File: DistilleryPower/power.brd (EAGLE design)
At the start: 50 x 86.9 mm, 31 parts, among them IC2 ACS758LCB-050B-PFF-T, J1 GREEN-2P-5.0, J2 GREEN-2P-5.0, Q1 BC807-16LT1SMD, T1 BT138-DSH, U1 STM32F042KXTX

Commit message: digital part schematics
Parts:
- added C10, C13: 10u/25, rcl:SMC_B
- added C11, C12: 20p, rcl:C0805
- added C14, C15, C18, C19, C6, C8: 0.1, rcl:C0805
- added C16, C17: (no value), rcl:C0805
- added C7: 100p, rcl:C0805
- added C9: 0.01/500, rcl:C1206
- added IC3: (no value), SparkFun:SOT223
- added IC4: ACS758LCB-050B-PFF-T, allegro:CB-PFF
- added J3, J4, J5: GREEN-2P-5.0, distillery:H2-5.0-10.5X8.0MM
- added R14: 220, rcl:R0805
- added R15: (no value), rcl:R0805
- added SV1: (no value), distillery:CON-LSTB_MA06-1
- added X1: IQD-FREQUENCY-PRODUCTS_CRYSTALS-NOGND-4-HSMX, distillery:IQD-FREQUENCY-PRODUCTS_HC49-4-HSMX
- C1: value 0.47/50 -> 0.1; device rcl:C/6032-28R -> rcl:C0805
- C2, C5: value (none) -> 0.1
- C3: value 0.01/500 -> 0.1; device rcl:C1206 -> rcl:C0805
- C4: value (none) -> 0.47/50; device rcl:C0805 -> rcl:C/6032-28R
- IC1: value (none) -> SN65HVD230/1; device SparkFun:SOT223 -> distillery:SO8
- IC2: value ACS758LCB-050B-PFF-T -> MICROCHIP_BY_ELEMENT14_BATCH_1_24LC16B-I/SN; device allegro:CB-PFF -> distillery:MICROCHIP_BY_ELEMENT14_BATCH_1_SOIC127P600X175-8N
- R13: value (none) -> 120/1%
- R6: value (none) -> 330
- R7: value (none) -> 2k2
- R8: value 330 -> 100
- R9: value 2k2 -> 100
- moved C3 357.9 mm to (-174.6, -238.1)
- moved C1 332.8 mm to (-174.6, -231.8), turned to 0 degrees
- moved IC2 324.1 mm to (-170.2, -197.5)
- moved R13 272.5 mm to (-174.6, -283.8)
- moved R8 258.2 mm to (-174.6, -273.1)
- moved C2 245.2 mm to (-174.6, -244.5)
- moved R9 174.2 mm to (-174.6, -277.5)
- moved R7 115.3 mm to (-78.7, -132.1)
- moved C4 93.6 mm to (17.1, 47.0), turned to 270 degrees
- moved IC1 91.5 mm to (-171.4, -259.1)
- moved J1 76.3 mm to (4.68, 5.65)
- moved R6 38.1 mm to (-29.2, -59.7)
- moved J2 15.2 mm to (14.8, 81.2)
- moved R10 7.10 mm to (36.8, 55.2)
- moved R12 7.10 mm to (40.6, 55.2)
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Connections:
- new net !NRST: C5.1, R5.1, SV1.5, U1.4
- new net CAN_RX: R9.2, U1.21
- new net CAN_TX: R8.2, U1.22
- new net I2C_SCL: IC2.6, U1.19
- new net I2C_SDA: IC2.5, U1.20
- new net N$13: C10.+, IC3.3, J1.1
- new net N$16: C12.2, R14.1, X1.2
- new net N$19: C1.1, C2.1, C3.1
- new net N$20: C18.1, C19.1, IC1.6, J4.1, J5.1, R13.1
- new net N$21: IC1.1, R8.1
- new net N$22: IC1.4, R9.1
- new net N$24: C14.1, C15.1, IC1.7, J4.2, J5.2, R13.2
- new net OSC_IN: C11.2, U1.2, X1.1
- new net OSC_OUT: R14.2, U1.3
- new net SWCLK: C7.2, SV1.2, U1.24
- new net SWDIO: SV1.4, U1.23
- net +3V3: now also C13.+, C17.1, C6.2, C8.2, IC1.3, IC2.8, IC3.2, IC3.4, IC4.1, R5.2, R6.1, R7.2, SV1.1, U1.1, U1.17, U1.5; no longer C5.1, IC2.1, R8.1, R9.2
- net 50HZ_0: now also IC4.IP-, IC4.IP-@10, IC4.IP-@11, IC4.IP-@12, IC4.IP-@13, IC4.IP-@14, IC4.IP-@15, IC4.IP-@16, IC4.IP-@17, IC4.IP-@2, IC4.IP-@3, IC4.IP-@4, IC4.IP-@5, IC4.IP-@6, IC4.IP-@7, IC4.IP-@8, IC4.IP-@9, J2.1; no longer IC2.IP-, IC2.IP-@10, IC2.IP-@11, IC2.IP-@12, IC2.IP-@13, IC2.IP-@14, IC2.IP-@15, IC2.IP-@16, IC2.IP-@17, IC2.IP-@2, IC2.IP-@3, IC2.IP-@4, IC2.IP-@5, IC2.IP-@6, IC2.IP-@7, IC2.IP-@8, IC2.IP-@9, J1.1
- net 50HZ_1: now also J2.2, J3.1; no longer J1.2, J2.1
- net CUR_LOAD: now also C16.1, R15.2; no longer C4.1, R13.2
- net GND: now also C1.2, C10.-, C11.1, C12.1, C13.-, C14.2, C15.2, C16.2, C17.2, C18.2, C19.2, C2.2, C3.2, C6.1, C7.1, C8.1, IC1.2, IC1.8, IC2.4, IC2.7, IC3.1, IC4.2, J1.2, SV1.3, U1.16, U1.31, U1.32; no longer C4.2, IC2.2
- net N$10: now also C9.1; no longer C3.1
- net N$14: now also R6.2; no longer R8.2
- net N$17: now also IC4.IP+, IC4.IP+@10, IC4.IP+@11, IC4.IP+@12, IC4.IP+@13, IC4.IP+@14, IC4.IP+@15, IC4.IP+@16, IC4.IP+@17, IC4.IP+@2, IC4.IP+@3, IC4.IP+@4, IC4.IP+@5, IC4.IP+@6, IC4.IP+@7, IC4.IP+@8, IC4.IP+@9; no longer IC2.IP+, IC2.IP+@10, IC2.IP+@11, IC2.IP+@12, IC2.IP+@13, IC2.IP+@14, IC2.IP+@15, IC2.IP+@16, IC2.IP+@17, IC2.IP+@2, IC2.IP+@3, IC2.IP+@4, IC2.IP+@5, IC2.IP+@6, IC2.IP+@7, IC2.IP+@8, IC2.IP+@9
- net N$18: now also C9.2, J3.2; no longer C3.2, J2.2
- net N$2: now also IC4.3, R15.1; no longer IC2.3, R13.1
- net N$5: now also C4.-; no longer C1.-
- net N$6: now also C4.+; no longer C1.+
- net SYNC: now also R7.1; no longer R9.1
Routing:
- net 50HZ_1: track 51.6 -> 44.7 mm
- net N$9: track 8.54 -> 10.3 mm
- net N$5: track 38.6 -> 40.4 mm
- net N$10: track 6.30 -> 7.57 mm
- net N$11: track 17.0 -> 18.3 mm
- net N$7: track 16.2 -> 15.2 mm
- net N$8: track 5.32 -> 4.68 mm
- net N$4: track 22.0 -> 22.5 mm
- net N$17: track 8.81 -> 8.28 mm

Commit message: power control board routing finished
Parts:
- added C20, C21: 0.1, rcl:C0603
- added R16, R17, R18, R19, R20, R21, R22, R23, R24, R25, R26: 100, rcl:R0603
- added X2: 2516-, con-3m:PAK100/2500-16
- C1, C11, C12, C14, C15, C16, C17, C18, C19, C2, C3, C5, C6, C7, C8: device rcl:C0805 -> rcl:C0603
- R13, R14, R15, R5, R6, R7, R8, R9: device rcl:R0805 -> rcl:R0603
- moved C15 414.9 mm to (36.2, 10.8), turned to 180 degrees
- moved C19 409.4 mm to (31.1, 10.8)
- moved J5 401.0 mm to (40.2, 5.65), turned to 90 degrees
- moved C18 400.7 mm to (40.6, 10.8)
- moved C14 398.2 mm to (45.1, 10.8)
- moved R9 370.4 mm to (29.3, 31.8), turned to 180 degrees
- moved R8 368.3 mm to (29.3, 33.7), turned to 180 degrees
- moved R13 366.2 mm to (39.4, 13.3)
- moved J4 363.8 mm to (30.1, 5.65), turned to 90 degrees
- moved C6 357.9 mm to (36.2, 22.5), turned to 270 degrees
- moved IC1 349.0 mm to (39.4, 19.1), turned to 180 degrees
- moved C8 347.3 mm to (32.2, 28.3)
- moved C3 334.5 mm to (27.7, 28.3), turned to 180 degrees
- moved C2 332.2 mm to (13.8, 29.2), turned to 90 degrees
- moved C1 327.3 mm to (14.3, 35.5), turned to 270 degrees
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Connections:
- removed net N$19: C1.1, C2.1, C3.1
- removed net SYNC: G1.4, R7.1
- new net A: R16.1, U1.6
- new net B: R17.1, U1.7
- new net C: R18.1, U1.8
- new net D: R19.1, U1.9
- new net DG0: R24.1, U1.27
- new net DG1: R25.1, U1.28
- new net DG2: R26.1, U1.29
- new net DP: R23.1, U1.13
- new net E: R20.1, U1.10
- new net F: R21.1, U1.11
- new net G: R22.1, U1.12
- new net N$15: R16.2, X2.3
- new net N$23: R17.2, X2.4
- new net N$25: R18.2, X2.5
- new net N$26: R19.2, X2.6
- new net N$27: R20.2, X2.7
- new net N$28: R21.2, X2.8
- new net N$29: R22.2, X2.9
- new net N$30: R23.2, X2.10
- new net N$31: R24.2, X2.11
- new net N$32: R25.2, X2.12
- new net N$33: R26.2, X2.13
- new net SW0: C20.2, U1.14, X2.14
- new net SW1: C21.2, U1.18, X2.15
- new net ZERO_CROSS: G1.4, R7.1, U1.30
- net +3V3: now also C1.2, C2.2, C3.2, X2.2; no longer R6.1
- net CUR_LOAD: now also U1.15
- net GND: now also C1.1, C2.1, C20.1, C21.1, C3.1, J1.1, R6.1, X2.1, X2.16; no longer C1.2, C2.2, C3.2, J1.2
- net N$13: now also J1.2; no longer J1.1
- net N$14: now also OK1.2; no longer OK1.1
- net N$20: now also C14.1, C15.1, J4.2, J5.2; no longer C18.1, C19.1, J4.1, J5.1
- net N$24: now also C18.1, C19.1, J4.1, J5.1; no longer C14.1, C15.1, J4.2, J5.2
- net PHASE_OUT: now also OK1.1, U1.25; no longer OK1.2
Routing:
- net +3V3: track 0.00 -> 248.3 mm
- net GND: track 0.00 -> 66.2 mm, vias 0 -> 23
- net !NRST: track 0.00 -> 36.8 mm
- net DG2: track 0.00 -> 30.2 mm, vias 0 -> 2
- net SWCLK: track 0.00 -> 30.0 mm
- net N$20: track 0.00 -> 29.7 mm
- net N$24: track 0.00 -> 28.7 mm
- net DG1: track 0.00 -> 26.7 mm, vias 0 -> 2
- net DG0: track 0.00 -> 23.7 mm, vias 0 -> 2
- net SW1: track 0.00 -> 23.7 mm
- net SWDIO: track 0.00 -> 23.7 mm, vias 0 -> 1
- net CUR_LOAD: track 0.00 -> 22.2 mm, vias 0 -> 2
- net SW0: track 0.00 -> 20.2 mm
- net N$21: track 0.00 -> 19.3 mm
- net N$22: track 0.00 -> 16.4 mm
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- added copper zone on layer 16, net GND
- removed copper zone on layer 16, net N$12

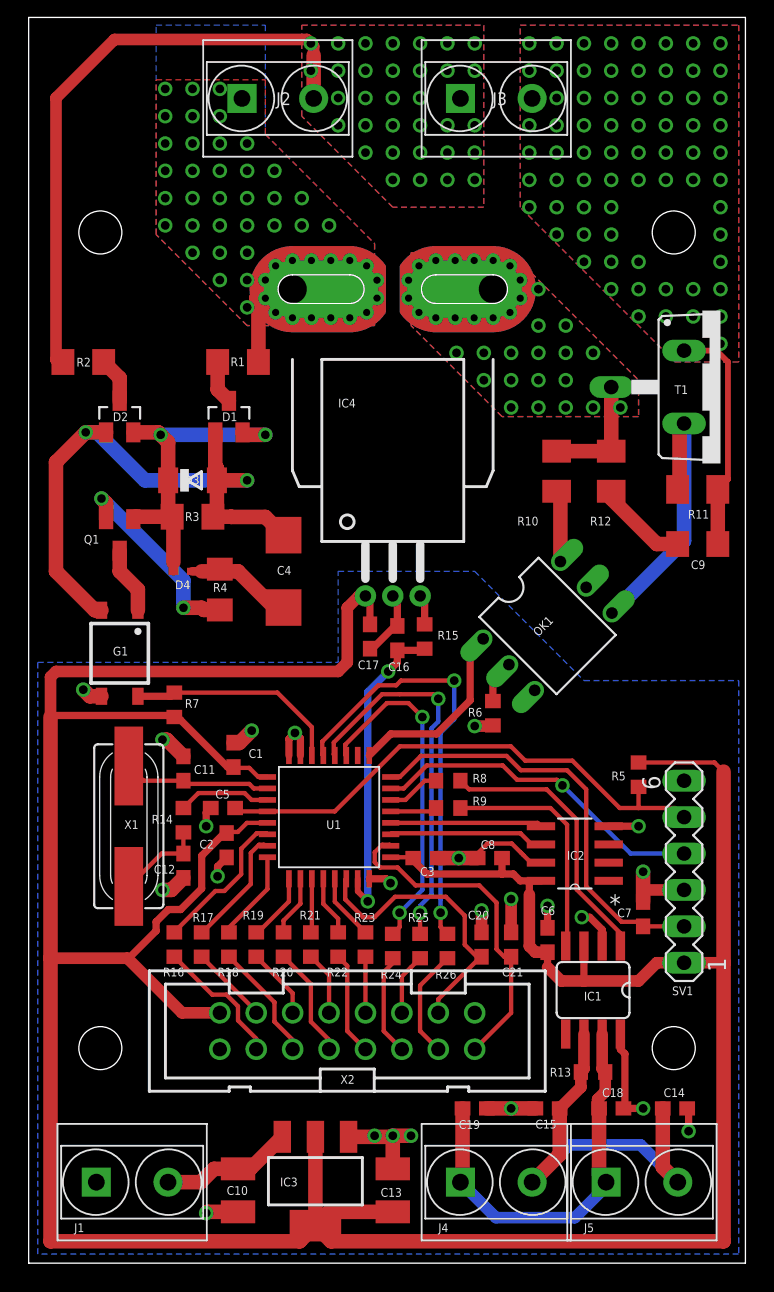
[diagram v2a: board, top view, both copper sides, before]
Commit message: export all to local library; renumber symbols;
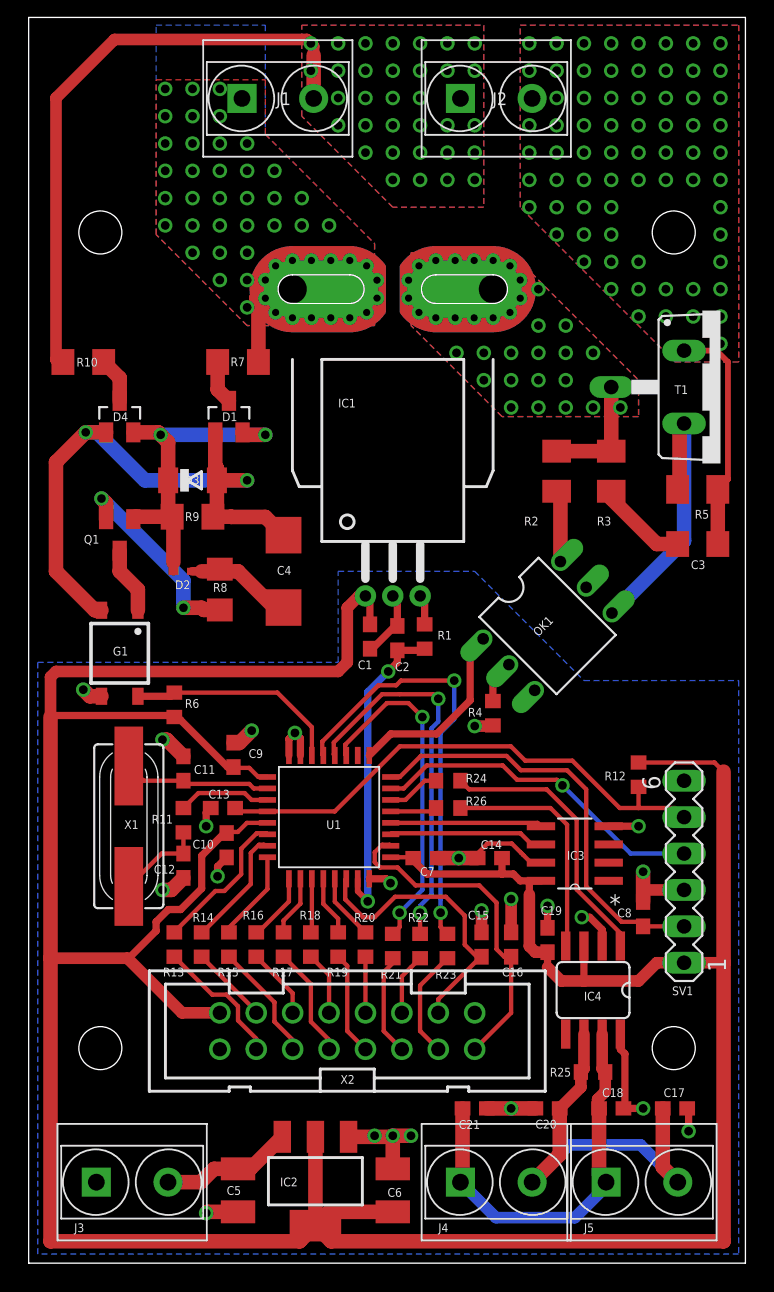
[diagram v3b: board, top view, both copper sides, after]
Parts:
- C1: value 0.1 -> (none)
- C10, C13: value 10u/25 -> 0.1; device rcl:SMC_B -> rcl:C0603
- C16, C17: value (none) -> 0.1
- C2: value 0.1 -> 68p
- C3: value 0.1 -> 0.01/500; device rcl:C0603 -> rcl:C1206
- C5, C6: value 0.1 -> 10u/25; device rcl:C0603 -> rcl:SMC_B
- C7: value 100p -> 0.1
- C8: value 0.1 -> 100p
- C9: value 0.01/500 -> 0.1; device rcl:C1206 -> rcl:C0603
- D2: value BAV199 -> (none); device diode:SOT23 -> diode:SOD523
- D4: value (none) -> BAV199; device diode:SOD523 -> diode:SOT23
- IC1: value SN65HVD230/1 -> ACS758LCB-050B-PFF-T; device distillery:SO8 -> allegro:CB-PFF
- IC2: value MICROCHIP_BY_ELEMENT14_BATCH_1_24LC16B-I/SN -> (none); device distillery:MICROCHIP_BY_ELEMENT14_BATCH_1_SOIC127P600X175-8N -> SparkFun:SOT223
- IC3: value (none) -> MICROCHIP_BY_ELEMENT14_BATCH_1_24LC16B-I/SN; device SparkFun:SOT223 -> distillery:MICROCHIP_BY_ELEMENT14_BATCH_1_SOIC127P600X175-8N
- IC4: value ACS758LCB-050B-PFF-T -> SN65HVD230/1; device allegro:CB-PFF -> distillery:SO8
- R1: value 120k -> 10k; device rcl:R1206 -> rcl:R0603
- R10: value 380/0.25 -> 120k; device rcl:M1206 -> rcl:R1206
- R11: value 330/0.25 -> 220; device rcl:M1206 -> rcl:R0603
- R12: value 39/0.25 -> (none); device rcl:M1206 -> rcl:R0603
- R13: value 120/1% -> 100
- R14: value 220 -> 100
- R15: value (none) -> 100
- R2: value 120k -> 380/0.25; device rcl:R1206 -> rcl:M1206
- R25: value 100 -> 120/1%
- R3: value 330k -> 39/0.25; device rcl:R1206 -> rcl:M1206
- R4: value 220 -> 330; device rcl:R1206 -> rcl:R0603
- R5: value (none) -> 330/0.25; device rcl:R0603 -> rcl:M1206
- R6: value 330 -> 2k2
- R7: value 2k2 -> 120k; device rcl:R0603 -> rcl:R1206
- R8: value 100 -> 220; device rcl:R0603 -> rcl:R1206
- R9: value 100 -> 330k; device rcl:R0603 -> rcl:R1206
- moved J3 79.8 mm to (4.68, 5.65)
- moved J1 76.3 mm to (14.8, 81.2)
- moved IC1 50.9 mm to (25.4, 67.9), turned to 0 degrees
- moved IC4 50.9 mm to (39.4, 19.1), turned to 180 degrees
- moved R11 42.7 mm to (10.8, 30.9), turned to 90 degrees
- moved C17 39.2 mm to (45.1, 10.8), turned to 0 degrees
- moved C9 35.6 mm to (14.3, 35.5), turned to 270 degrees
- moved R10 33.9 mm to (3.81, 62.9), turned to 0 degrees
- moved R2 33.9 mm to (36.8, 55.2), turned to 90 degrees
- moved R13 30.5 mm to (10.2, 22.2), turned to 270 degrees
- moved R3 29.4 mm to (40.6, 55.2), turned to 90 degrees
- moved C13 29.2 mm to (13.6, 31.8), turned to 180 degrees
- moved IC2 29.2 mm to (20.0, 5.71)
- moved IC3 29.2 mm to (38.1, 28.6)
- moved C3 29.0 mm to (46.7, 50.2), turned to 0 degrees
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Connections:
- net !NRST: now also C13.1, R12.1; no longer C5.1, R5.1
- net +3V3: now also C1.1, C10.2, C14.2, C19.2, C6.+, C7.2, C9.2, IC1.1, IC2.2, IC2.4, IC3.8, IC4.3, R12.2, R6.2; no longer C1.2, C13.+, C17.1, C2.2, C3.2, C6.2, C8.2, IC1.3, IC2.8, IC3.2, IC3.4, IC4.1, R5.2, R7.2
- net 50HZ_0: now also IC1.IP-, IC1.IP-@10, IC1.IP-@11, IC1.IP-@12, IC1.IP-@13, IC1.IP-@14, IC1.IP-@15, IC1.IP-@16, IC1.IP-@17, IC1.IP-@2, IC1.IP-@3, IC1.IP-@4, IC1.IP-@5, IC1.IP-@6, IC1.IP-@7, IC1.IP-@8, IC1.IP-@9, J1.1, R7.1; no longer IC4.IP-, IC4.IP-@10, IC4.IP-@11, IC4.IP-@12, IC4.IP-@13, IC4.IP-@14, IC4.IP-@15, IC4.IP-@16, IC4.IP-@17, IC4.IP-@2, IC4.IP-@3, IC4.IP-@4, IC4.IP-@5, IC4.IP-@6, IC4.IP-@7, IC4.IP-@8, IC4.IP-@9, J2.1, R1.1
- net 50HZ_1: now also J1.2, J2.1, R10.1; no longer J2.2, J3.1, R2.1
- net A: now also R13.1; no longer R16.1
- net B: now also R14.1; no longer R17.1
- net C: now also R15.1; no longer R18.1
- net CAN_RX: now also R26.2; no longer R9.2
- net CAN_TX: now also R24.2; no longer R8.2
- net CUR_LOAD: now also C2.1, R1.2; no longer C16.1, R15.2
- net D: now also R16.1; no longer R19.1
- net DG0: now also R21.1; no longer R24.1
- net DG1: now also R22.1; no longer R25.1
- net DG2: now also R23.1; no longer R26.1
- net DP: now also R20.1; no longer R23.1
- net E: now also R17.1; no longer R20.1
- net F: now also R18.1; no longer R21.1
- net G: now also R19.1; no longer R22.1
- net GND: now also C1.2, C10.1, C13.2, C14.1, C15.1, C16.1, C19.1, C2.2, C20.2, C21.2, C5.-, C6.-, C9.1, IC2.1, IC3.4, IC3.7, IC4.8, J3.1, R4.1; no longer C1.1, C10.-, C13.-, C14.2, C15.2, C16.2, C19.2, C2.1, C20.1, C21.1, C3.1, C5.2, C6.1, IC1.8, IC2.4, IC2.7, IC3.1, J1.1, R6.1
- net I2C_SCL: now also IC3.6; no longer IC2.6
- net I2C_SDA: now also IC3.5; no longer IC2.5
- net N$1: now also R7.2; no longer R1.2
- net N$10: now also C3.1, R3.1; no longer C9.1, R12.1
- net N$11: now also R5.2; no longer R11.2
- net N$13: now also C5.+, IC2.3, J3.2; no longer C10.+, IC3.3, J1.2
- net N$14: now also R4.2; no longer R6.2
- net N$15: now also R13.2; no longer R16.2
- net N$16: now also R11.1; no longer R14.1
- net N$17: now also IC1.IP+, IC1.IP+@10, IC1.IP+@11, IC1.IP+@12, IC1.IP+@13, IC1.IP+@14, IC1.IP+@15, IC1.IP+@16, IC1.IP+@17, IC1.IP+@2, IC1.IP+@3, IC1.IP+@4, IC1.IP+@5, IC1.IP+@6, IC1.IP+@7, IC1.IP+@8, IC1.IP+@9, R2.2, R3.2; no longer IC4.IP+, IC4.IP+@10, IC4.IP+@11, IC4.IP+@12, IC4.IP+@13, IC4.IP+@14, IC4.IP+@15, IC4.IP+@16, IC4.IP+@17, IC4.IP+@2, IC4.IP+@3, IC4.IP+@4, IC4.IP+@5, IC4.IP+@6, IC4.IP+@7, IC4.IP+@8, IC4.IP+@9, R10.2, R12.2
- net N$18: now also C3.2, J2.2, R5.1; no longer C9.2, J3.2, R11.1
- net N$2: now also IC1.3, R1.1; no longer IC4.3, R15.1
- net N$20: now also C17.1, C20.1, IC4.6, R25.1; no longer C14.1, C15.1, IC1.6, R13.1
- net N$21: now also IC4.1, R24.1; no longer IC1.1, R8.1
- net N$22: now also IC4.4, R26.1; no longer IC1.4, R9.1
- net N$23: now also R14.2; no longer R17.2
- net N$24: now also C21.1, IC4.7, R25.2; no longer C19.1, IC1.7, R13.2
- net N$25: now also R15.2; no longer R18.2
- net N$26: now also R16.2; no longer R19.2
- net N$27: now also R17.2; no longer R20.2
- net N$28: now also R18.2; no longer R21.2
- net N$29: now also R19.2; no longer R22.2
- net N$3: now also D4.3, R10.2; no longer D2.3, R2.2
- net N$30: now also R20.2; no longer R23.2
- net N$31: now also R21.2; no longer R24.2
- net N$32: now also R22.2; no longer R25.2
- net N$33: now also R23.2; no longer R26.2
- net N$4: now also D2.A, D4.2, R9.2; no longer D2.2, D4.A, R3.2
- net N$5: now also D4.1, R9.1; no longer D2.1, R3.1
- net N$6: now also D2.C, R8.1; no longer D4.C, R4.1
- net N$7: now also R8.2; no longer R4.2
- net N$9: now also R2.1; no longer R10.1
- net OSC_OUT: now also R11.2; no longer R14.2
- net SW0: now also C15.2; no longer C20.2
- net SW1: now also C16.2; no longer C21.2
- net SWCLK: now also C8.2; no longer C7.2
- net ZERO_CROSS: now also R6.1; no longer R7.1
